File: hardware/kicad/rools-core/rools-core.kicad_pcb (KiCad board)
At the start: 4 copper layers, 50.3 x 128.5 mm, 0 parts

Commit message: Lay out Core front-panel PCB for 10HP Eurorack fit.
Use RK09L 3-pin no-MP pots, split Daisy daughterboard, audio jack refs, and local display footprint library.

Co-authored-by: Cursor <cursoragent@cursor.com>
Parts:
- added C1: 10uF, Capacitor_SMD:C_0603_1608Metric, F.Cu at (121.9, -49.6)
- added C10: 22uF, Capacitor_SMD:C_0805_2012Metric, F.Cu at (143.8, -58.7)
- added C12: 100nF, Capacitor_SMD:C_0603_1608Metric, F.Cu at (169.1, -141.2)
- added C13: 100nF, Capacitor_SMD:C_0603_1608Metric, F.Cu at (169.1, -138.7)
- added C14: 10nF, Capacitor_SMD:C_0603_1608Metric, F.Cu at (169.1, -136.2)
- added C15: 10nF, Capacitor_SMD:C_0603_1608Metric, F.Cu at (169.1, -133.7)
- added C16: 10nF, Capacitor_SMD:C_0603_1608Metric, F.Cu at (169.1, -131.2)
- added C17: 10nF, Capacitor_SMD:C_0603_1608Metric, F.Cu at (169.1, -128.7)
- added C18: 100nF, Capacitor_SMD:C_0603_1608Metric, F.Cu at (169.1, -126.1)
- added C19: 100nF, Capacitor_SMD:C_0603_1608Metric, F.Cu at (169.1, -123.6)
- added C2: 100nF, Capacitor_SMD:C_0603_1608Metric, F.Cu at (121.9, -47.1)
- added C20: 100nF, Capacitor_SMD:C_0603_1608Metric, F.Cu at (201.0, -113.8)
- added C21: 47pF, Capacitor_SMD:C_0603_1608Metric, F.Cu at (109.9, -98.3)
- added C22: 560pF, Capacitor_SMD:C_0603_1608Metric, F.Cu at (109.9, -95.8)
- added C23: 47pF, Capacitor_SMD:C_0603_1608Metric, F.Cu at (109.9, -93.3)
- added C24: 560pF, Capacitor_SMD:C_0603_1608Metric, F.Cu at (109.9, -90.8)
- added C25: 100nF, Capacitor_SMD:C_0603_1608Metric, F.Cu at (109.9, -88.3)
- added C26: 100nF, Capacitor_SMD:C_0603_1608Metric, F.Cu at (109.9, -85.8)
- added C27: 47pF, Capacitor_SMD:C_0603_1608Metric, F.Cu at (109.9, -83.3)
- added C28: 47pF, Capacitor_SMD:C_0603_1608Metric, F.Cu at (109.9, -80.8)
- added C29: 47pF, Capacitor_SMD:C_0603_1608Metric, F.Cu at (109.9, -78.3)
- added C3: 100nF, Capacitor_SMD:C_0603_1608Metric, F.Cu at (121.9, -44.6)
- added C30: 47pF, Capacitor_SMD:C_0603_1608Metric, F.Cu at (113.9, -98.3)
- added C31: 100nF, Capacitor_SMD:C_0603_1608Metric, F.Cu at (113.9, -95.8)
- added C32: 100nF, Capacitor_SMD:C_0603_1608Metric, F.Cu at (113.9, -93.3)
- added C33: 100nF, Capacitor_SMD:C_0603_1608Metric, F.Cu at (169.1, -121.1)
- added C34: 100nF, Capacitor_SMD:C_0603_1608Metric, F.Cu at (173.1, -141.2)
- added C35: 100nF, Capacitor_SMD:C_0603_1608Metric, F.Cu at (173.1, -138.7)
- added C36: 1000uF/25V, Capacitor_SMD:CP_Elec_10x10.5, F.Cu at (127.3, -69.0)
- added C37: 1000uF/25V, Capacitor_SMD:CP_Elec_10x10.5, F.Cu at (127.3, -56.9)
- added C4: 10uF, Capacitor_SMD:C_0603_1608Metric, F.Cu at (121.9, -42.1)
- added C5: 10uF, Capacitor_SMD:C_0603_1608Metric, F.Cu at (121.9, -39.6)
- added C6: 10uF, Capacitor_SMD:C_0603_1608Metric, F.Cu at (121.9, -37.1)
- added C7: 10uF, Capacitor_SMD:C_0603_1608Metric, F.Cu at (121.9, -34.6)
- added C8: 10uF, Capacitor_SMD:C_0603_1608Metric, F.Cu at (125.9, -49.6)
- added C9: 100nF, Capacitor_SMD:C_0603_1608Metric, F.Cu at (125.9, -47.1)
- added D1: SS34, Diode_SMD:D_SMA, F.Cu at (140.5, -48.6)
- added D2: SS34, Diode_SMD:D_SMA, F.Cu at (140.5, -44.1)
- added D3: SS34, Diode_SMD:D_SMA, F.Cu at (140.5, -39.5)
- added FB1: FerriteBead, Inductor_SMD:L_0603_1608Metric, F.Cu at (125.9, -44.6)
- added FB2: FerriteBead, Inductor_SMD:L_0603_1608Metric, F.Cu at (125.9, -42.1)
- added J1: EURO_PWR, Connector_IDC:IDC-Header_2x05_P2.54mm_Vertical, B.Cu at (156.6, 145.9)
- added J2: EXP_BUS, Connector_PinHeader_2.54mm:PinHeader_2x08_P2.54mm_Vertical, B.Cu at (194.1, 125.9)
- added J3: DEBUG_SWD, Connector_PinHeader_2.54mm:PinHeader_1x05_P2.54mm_Vertical, F.Cu at (134.2, -48.6)
- added J4: ST7789, Library:Display_1.54in_240x240, F.Cu at (124.1, 63.7)
- added J_AI_L1: AudioJack2_SwitchT, Connector_Audio:Jack_3.5mm_QingPu_WQP-PJ398SM_Vertical_CircularHoles, F.Cu at (105.6, 144.6)
- added J_AI_R1: AudioJack2_SwitchT, Connector_Audio:Jack_3.5mm_QingPu_WQP-PJ398SM_Vertical_CircularHoles, F.Cu at (117.9, 144.6)
- added J_AO_L1: AudioJack2_SwitchT, Connector_Audio:Jack_3.5mm_QingPu_WQP-PJ398SM_Vertical_CircularHoles, F.Cu at (130.3, 144.6)
- added J_AO_R1: AudioJack2_SwitchT, Connector_Audio:Jack_3.5mm_QingPu_WQP-PJ398SM_Vertical_CircularHoles, F.Cu at (142.6, 144.6)
- added J_CV_IN_1: AudioJack2_SwitchT, Connector_Audio:Jack_3.5mm_QingPu_WQP-PJ398SM_Vertical_CircularHoles, F.Cu at (105.6, 115.9)
- added J_CV_IN_2: AudioJack2_SwitchT, Connector_Audio:Jack_3.5mm_QingPu_WQP-PJ398SM_Vertical_CircularHoles, F.Cu at (117.9, 116.0)
- added J_CV_IN_3: AudioJack2_SwitchT, Connector_Audio:Jack_3.5mm_QingPu_WQP-PJ398SM_Vertical_CircularHoles, F.Cu at (130.3, 115.9)
- added J_CV_IN_4: AudioJack2_SwitchT, Connector_Audio:Jack_3.5mm_QingPu_WQP-PJ398SM_Vertical_CircularHoles, F.Cu at (142.6, 115.9)
- added J_CV_OUT_1: AudioJack2_SwitchT, Connector_Audio:Jack_3.5mm_QingPu_WQP-PJ398SM_Vertical_CircularHoles, F.Cu at (105.6, 130.2)
- added J_CV_OUT_2: AudioJack2_SwitchT, Connector_Audio:Jack_3.5mm_QingPu_WQP-PJ398SM_Vertical_CircularHoles, F.Cu at (117.9, 130.2)
- added J_CV_OUT_3: AudioJack2_SwitchT, Connector_Audio:Jack_3.5mm_QingPu_WQP-PJ398SM_Vertical_CircularHoles, F.Cu at (130.3, 130.2)
- added J_CV_OUT_4: AudioJack2_SwitchT, Connector_Audio:Jack_3.5mm_QingPu_WQP-PJ398SM_Vertical_CircularHoles, F.Cu at (142.6, 130.2)
- added L1: 4.7uH, Inductor_SMD:L_Taiyo-Yuden_NR-40xx, F.Cu at (144.3, -63.0)
- added R1: 330K, Resistor_SMD:R_0603_1608Metric, F.Cu at (125.9, -39.6)
- added R10: 120K, Resistor_SMD:R_0603_1608Metric, F.Cu at (173.1, -128.7)
- added R11: 15K, Resistor_SMD:R_0603_1608Metric, F.Cu at (173.1, -126.1)
- added R12: 120K, Resistor_SMD:R_0603_1608Metric, F.Cu at (173.1, -123.6)
- added R13: 15K, Resistor_SMD:R_0603_1608Metric, F.Cu at (173.1, -121.1)
- added R14: 120K, Resistor_SMD:R_0603_1608Metric, F.Cu at (177.1, -141.2)
- added R15: 120K, Resistor_SMD:R_0603_1608Metric, F.Cu at (177.1, -138.7)
- added R16: 120K, Resistor_SMD:R_0603_1608Metric, F.Cu at (177.1, -136.2)
- added R17: 120K, Resistor_SMD:R_0603_1608Metric, F.Cu at (177.1, -133.7)
- added R18: 120K, Resistor_SMD:R_0603_1608Metric, F.Cu at (177.1, -131.2)
- added R19: 1K, Resistor_SMD:R_0603_1608Metric, F.Cu at (177.1, -128.7)
- added R2: 100K, Resistor_SMD:R_0603_1608Metric, F.Cu at (125.9, -37.1)
- added R20: 1K, Resistor_SMD:R_0603_1608Metric, F.Cu at (177.1, -126.1)
- added R21: 1K, Resistor_SMD:R_0603_1608Metric, F.Cu at (177.1, -123.6)
- added R22: 1K, Resistor_SMD:R_0603_1608Metric, F.Cu at (177.1, -121.1)
- added R23: 200K, Resistor_SMD:R_0603_1608Metric, F.Cu at (181.1, -141.2)
- added R24: 200K, Resistor_SMD:R_0603_1608Metric, F.Cu at (181.1, -138.7)
- added R25: 200K, Resistor_SMD:R_0603_1608Metric, F.Cu at (181.1, -136.2)
- added R26: 200K, Resistor_SMD:R_0603_1608Metric, F.Cu at (181.1, -133.7)
- added R27: 200K, Resistor_SMD:R_0603_1608Metric, F.Cu at (181.1, -131.2)
- added R28: 200K, Resistor_SMD:R_0603_1608Metric, F.Cu at (181.1, -128.7)
- added R29: 200K, Resistor_SMD:R_0603_1608Metric, F.Cu at (181.1, -126.1)
- added R3: 10K, Resistor_SMD:R_0603_1608Metric, F.Cu at (125.9, -34.6)
- added R30: 200K, Resistor_SMD:R_0603_1608Metric, F.Cu at (181.1, -123.6)
- added R31: 33K, Resistor_SMD:R_0603_1608Metric, F.Cu at (181.1, -121.1)
- added R32: 33K, Resistor_SMD:R_0603_1608Metric, F.Cu at (185.1, -141.2)
- added R33: 33K, Resistor_SMD:R_0603_1608Metric, F.Cu at (185.1, -138.7)
- added R34: 33K, Resistor_SMD:R_0603_1608Metric, F.Cu at (185.1, -136.2)
- added R35: 2K, Resistor_SMD:R_0603_1608Metric, F.Cu at (185.1, -133.7)
- added R36: 10K, Resistor_SMD:R_0603_1608Metric, F.Cu at (201.0, -111.3)
- added R37: 10K, Resistor_SMD:R_0603_1608Metric, F.Cu at (201.0, -108.8)
- added R38: 10K, Resistor_SMD:R_0603_1608Metric, F.Cu at (201.0, -106.3)
- added R39: 10K, Resistor_SMD:R_0603_1608Metric, F.Cu at (201.0, -103.8)
- added R4: 73.2K, Resistor_SMD:R_0603_1608Metric, F.Cu at (129.9, -49.6)
- added R40: 10K, Resistor_SMD:R_0603_1608Metric, F.Cu at (201.0, -101.2)
- added R41: 10K, Resistor_SMD:R_0603_1608Metric, F.Cu at (201.0, -98.7)
- added R42: 10K, Resistor_SMD:R_0603_1608Metric, F.Cu at (201.0, -96.2)
- added R43: 22K, Resistor_SMD:R_0603_1608Metric, F.Cu at (129.9, -47.1)
- added R44: 100K, Resistor_SMD:R_0603_1608Metric, F.Cu at (113.9, -90.8)
- added R45: 100K, Resistor_SMD:R_0603_1608Metric, F.Cu at (113.9, -88.3)
- added R46: 100K, Resistor_SMD:R_0603_1608Metric, F.Cu at (113.9, -85.8)
- added R47: 10K, Resistor_SMD:R_0603_1608Metric, F.Cu at (113.9, -83.3)
- added R48: 1K, Resistor_SMD:R_0603_1608Metric, F.Cu at (113.9, -80.8)
- added R49: 100K, Resistor_SMD:R_0603_1608Metric, F.Cu at (113.9, -78.3)
- added R50: 100K, Resistor_SMD:R_0603_1608Metric, F.Cu at (117.9, -98.3)
- added R51: 100K, Resistor_SMD:R_0603_1608Metric, F.Cu at (117.9, -95.8)
- added R52: 10K, Resistor_SMD:R_0603_1608Metric, F.Cu at (117.9, -93.3)
- added R53: 1K, Resistor_SMD:R_0603_1608Metric, F.Cu at (117.9, -90.8)
- added R54: 10K, Resistor_SMD:R_0603_1608Metric, F.Cu at (117.9, -88.3)
- added R55: 10K, Resistor_SMD:R_0603_1608Metric, F.Cu at (117.9, -85.8)
- added R56: 100K, Resistor_SMD:R_0603_1608Metric, F.Cu at (117.9, -83.3)
- added R57: 100K, Resistor_SMD:R_0603_1608Metric, F.Cu at (117.9, -80.8)
- added R58: 100K, Resistor_SMD:R_0603_1608Metric, F.Cu at (117.9, -78.3)
- added R59: 100K, Resistor_SMD:R_0603_1608Metric, F.Cu at (121.9, -98.3)
- added R60: 100K, Resistor_SMD:R_0603_1608Metric, F.Cu at (121.9, -95.8)
- added R61: 100K, Resistor_SMD:R_0603_1608Metric, F.Cu at (121.9, -93.3)
- added R62: 1K, Resistor_SMD:R_0603_1608Metric, F.Cu at (121.9, -90.8)
- added R63: 1K, Resistor_SMD:R_0603_1608Metric, F.Cu at (121.9, -88.3)
- added R64: 10K, Resistor_SMD:R_0603_1608Metric, F.Cu at (129.9, -44.6)
- added R65: 10K, Resistor_SMD:R_0603_1608Metric, F.Cu at (129.9, -42.1)
- added R7: 15K, Resistor_SMD:R_0603_1608Metric, F.Cu at (173.1, -136.2)
- added R8: 120K, Resistor_SMD:R_0603_1608Metric, F.Cu at (173.1, -133.7)
- added R9: 15K, Resistor_SMD:R_0603_1608Metric, F.Cu at (173.1, -131.2)
- added REF**: PinHeader_1x08_P2.54mm_Vertical_SMD_Pin1Right, Connector_PinHeader_2.54mm:PinHeader_1x08_P2.54mm_Vertical_SMD_Pin1Right, B.Cu at (142.4, 64.1)
- added REF**: PinHeader_1x08_P2.54mm_Vertical_SMD_Pin1Right, Connector_PinHeader_2.54mm:PinHeader_1x08_P2.54mm_Vertical_SMD_Pin1Right, B.Cu at (124.1, 99.4)
- added RV1: Knob, Potentiometer_THT:RK09L_3pin_noMP, F.Cu at (105.6, 99.3)
- added RV2: Knob, Potentiometer_THT:RK09L_3pin_noMP, F.Cu at (117.9, 99.3)
- added RV3: Knob, Potentiometer_THT:RK09L_3pin_noMP, F.Cu at (130.3, 99.3)
- added RV4: Knob, Potentiometer_THT:RK09L_3pin_noMP, F.Cu at (142.6, 99.3)
- added SW1: RotaryEncoder_Switch, Rotary_Encoder:RotaryEncoder_Alps_EC11E-Switch_Vertical_H20mm, F.Cu at (110.6, 87.2)
- added SW2: RotaryEncoder_Switch, Rotary_Encoder:RotaryEncoder_Alps_EC11E-Switch_Vertical_H20mm, F.Cu at (137.6, 87.2)
- added SW3: SW_Push, Button_Switch_THT:SW_PUSH_6mm, F.Cu at (124.1, 87.2)
- added U1: AP2112K-3.3, Package_TO_SOT_SMD:SOT-23-5, F.Cu at (144.2, -72.6)
- added U10: LM393, Package_SO:SOIC-8_3.9x4.9mm_P1.27mm, F.Cu at (112.1, -41.6)
- added U2: TPS54302, Package_TO_SOT_SMD:TSOT-23-6, F.Cu at (144.2, -68.0)
- added U4: OPA4171, Package_SO:SOIC-14_3.9x8.7mm_P1.27mm, F.Cu at (112.1, -122.1)
- added U5: MCP6004, Package_SO:SOIC-14_3.9x8.7mm_P1.27mm, F.Cu at (120.5, -122.1)
- added U6: LM4040DBZ-10, Package_TO_SOT_SMD:SOT-23, F.Cu at (136.3, -125.2)
- added U7: TL074, Package_SO:SOIC-14_3.9x8.7mm_P1.27mm, F.Cu at (128.1, -94.3)
- added U8: TL074, Package_SO:SOIC-14_3.9x8.7mm_P1.27mm, F.Cu at (136.6, -94.3)
- added U9: DAC8565, Package_SO:TSSOP-16_4.4x5mm_P0.65mm, F.Cu at (129.5, -124.1)
- added U_Daisy1: ES_DAISY_SEED, Module:Electrosmith_Daisy_Seed, B.Cu at (184.8, 50.3)
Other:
- board size 50.3 x 128.5 mm -> 102 x 108 mm

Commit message: Route Core PCB and place Daisy Seed on the daughterboard.
Sync schematic sheets with the split-board layout and updated interconnects.

Co-authored-by: Cursor <cursoragent@cursor.com>
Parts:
- removed C37: 1000uF/25V, Capacitor_SMD:CP_Elec_10x10.5
- removed REF** (x2): PinHeader_1x08_P2.54mm_Vertical_SMD_Pin1Right, Connector_PinHeader_2.54mm:PinHeader_1x08_P2.54mm_Vertical_SMD_Pin1Right
- added C11: 10uF, Capacitor_SMD:C_0603_1608Metric, B.Cu at (160.2, 108.7)
- added C38: 100nF, Capacitor_SMD:C_0603_1608Metric, B.Cu at (160.2, 110.4)
- added J5: J_BOT_UI, Connector_PinHeader_2.54mm:PinHeader_2x10_P2.54mm_Vertical_SMD, B.Cu at (124.1, 130.9)
- added J6: J_TOP_UI, Connector_PinHeader_2.54mm:PinHeader_2x08_P2.54mm_Vertical_SMD, B.Cu at (124.1, 63.6)
- added J7: J_TOP_MAIN, Connector_PinSocket_2.54mm:PinSocket_2x08_P2.54mm_Vertical_SMD, F.Cu at (176.1, 63.6)
- added J8: J_BOT_MAIN, Connector_PinSocket_2.54mm:PinSocket_2x10_P2.54mm_Vertical_SMD, F.Cu at (176.1, 130.9)
- C10, C20, C33, C34, C35, C4, C5, C7, C8, C9, D1, D2, D3, FB1, FB2, J3, L1, R1, R11, R13, R18, R19, R2, R22, R3, R4, R42, R43, R64, R65, R7, R9, U10, U2, U4, U9: moved to B.Cu
- C36: value 1000uF/25V -> 470uF/25V; footprint Capacitor_SMD:CP_Elec_10x10.5 -> Capacitor_THT:CP_Radial_D8.0mm_P3.50mm; moved to B.Cu
- moved C35 282.3 mm to (196.2, 142.6), turned to 180 degrees
- moved R7 280.4 mm to (184.1, 144.0), turned to 90 degrees
- moved U9 279.7 mm to (188.6, 149.3), turned to -90 degrees
- moved R9 275.4 mm to (186.3, 143.9), turned to 90 degrees
- moved C34 274.8 mm to (195.8, 132.7), turned to 90 degrees
- moved R11 270.9 mm to (192.6, 144.0), turned to 90 degrees
- moved U4 270.8 mm to (188.8, 137.6), turned to 180 degrees
- moved R18 266.4 mm to (181.8, 135.2), turned to 90 degrees
- moved R13 265.7 mm to (189.5, 144.0), turned to 90 degrees
- moved R19 259.9 mm to (190.0, 131.0)
- moved C33 255.0 mm to (194.2, 132.6), turned to 90 degrees
- moved R22 253.2 mm to (183.6, 132.0), turned to 180 degrees
- moved D1 196.9 mm to (160.1, 147.3), turned to 180 degrees
- moved C4 196.0 mm to (165.8, 148.9)
- moved FB1 194.1 mm to (154.8, 147.3)
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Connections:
- net Net-(J_AI_R1-PadS) renamed J_AUDIO_IN_R
- net Net-(J_AO_L1-PadS) renamed J_AUDIO_OUT_L
- net Net-(J_AO_R1-PadS) renamed J_AUDIO_OUT_R
- net Net-(J_CV_IN_1-PadS) renamed J_CV_IN_1
- net Net-(J_CV_IN_2-PadS) renamed J_CV_IN_2
- net Net-(J_CV_IN_3-PadS) renamed J_CV_IN_3
- net Net-(J_CV_IN_4-PadS) renamed J_CV_IN_4
- net Net-(J_CV_OUT_1-PadS) renamed J_CV_OUT_1
- net Net-(J_CV_OUT_2-PadS) renamed J_CV_OUT_2
- net Net-(J_CV_OUT_3-PadS) renamed J_CV_OUT_3
- net Net-(J_CV_OUT_4-PadS) renamed J_CV_OUT_4
- FB1 pad 1: Net-(J1-Pin_10) -> /Power/+12V_IN
- FB2 pad 1: Net-(J1-Pin_2) -> /Power/-12V_IN
- J1 pad 1: unconnected-(J1-Pin_1-Pad1) -> /Power/-12V_IN
- J1 pad 10: Net-(J1-Pin_10) -> /Power/+12V_IN
- J1 pad 2: Net-(J1-Pin_2) -> /Power/-12V_IN
- J1 pad 3: unconnected-(J1-Pin_3-Pad3) -> GND
- J1 pad 4: unconnected-(J1-Pin_4-Pad4) -> GND
- J1 pad 5: unconnected-(J1-Pin_5-Pad5) -> GND
- J1 pad 6: unconnected-(J1-Pin_6-Pad6) -> GND
- J1 pad 7: unconnected-(J1-Pin_7-Pad7) -> GND
- J1 pad 9: unconnected-(J1-Pin_9-Pad9) -> /Power/+12V_IN
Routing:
- net GND: track 0.00 -> 54.3 mm, vias 0 -> 23
- net ENC_A_B: track 0.00 -> 51.9 mm, vias 0 -> 1
- net EXTI_PWR: track 0.00 -> 50.7 mm
- net ENC_A_A: track 0.00 -> 47.6 mm, vias 0 -> 1
- net ENC_A_SW: track 0.00 -> 43.6 mm, vias 0 -> 1
- net BTN_CENTER: track 0.00 -> 41.4 mm, vias 0 -> 1
- net ENC_B_B: track 0.00 -> 36.9 mm
- net +12V_SAFE: track 0.00 -> 36.1 mm
- net +3V3_A: track 0.00 -> 32.2 mm
- net ENC_B_A: track 0.00 -> 29.0 mm
- net SPI1_MOSI: track 0.00 -> 25.8 mm, vias 0 -> 1
- net +3V3_D: track 0.00 -> 25.8 mm
- net SPI1_SCK: track 0.00 -> 25.5 mm, vias 0 -> 1
- net LCD_CS: track 0.00 -> 24.9 mm
- net LCD_RST: track 0.00 -> 23.8 mm
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- added copper zone on In1.Cu, net GND

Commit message: Remove Patch reference assets and continue Core PCB routing.
Drop imported Patch symbols, local display footprint, and stale BOM CSV while advancing layout and schematic interconnects.

Co-authored-by: Cursor <cursoragent@cursor.com>
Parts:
- C1, C12, C13, C19, C2, C21, C22, C23, C24, C25, C26, C27, C28, C29, C3, C30, C31, C32, C6, R10, R12, R14, R15, R16, R17, R20, R21, R35, R36, R37, R38, R39, R40, R41, R44, R45, R46, R47, R48, R49, R50, R51, R52, R53, R54, R55, R56, R57, R58, R59, R60, R61, R62, R63, R8, U1, U6, U7, U8: moved to B.Cu
- moved R35 262.3 mm to (178.3, 128.5)
- moved R15 259.8 mm to (168.8, 121.0), turned to -90 degrees
- moved R14 258.6 mm to (185.4, 117.3), turned to 180 degrees
- moved C12 258.1 mm to (170.7, 116.9), turned to 90 degrees
- moved C13 256.0 mm to (181.4, 117.1), turned to -90 degrees
- moved U6 255.5 mm to (174.3, 127.5), turned to 180 degrees
- moved C19 254.7 mm to (175.3, 131.0), turned to -90 degrees
- moved R8 250.9 mm to (166.5, 117.2)
- moved R16 249.3 mm to (168.8, 113.0), turned to 90 degrees
- moved R17 246.8 mm to (183.0, 113.1), turned to 90 degrees
- moved R10 244.2 mm to (166.5, 115.5)
- moved R33 242.1 mm to (187.6, 103.4), turned to 180 degrees
- moved R34 240.2 mm to (198.3, 103.6)
- moved R12 239.6 mm to (185.3, 115.6), turned to 180 degrees
- moved R20 239.2 mm to (170.4, 113.0), turned to -90 degrees
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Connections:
- J5 pad 10: J_CV_OUT_4 -> J_CV_IN_1
- J5 pad 11: J_CV_IN_1 -> J_CV_OUT_3
- J5 pad 12: J_CV_IN_2 -> J_CV_OUT_2
- J5 pad 13: J_CV_IN_3 -> J_CV_OUT_4
- J5 pad 14: J_CV_IN_4 -> J_CV_OUT_1
- J5 pad 15: IN_L_NORM -> J_AUDIO_OUT_R
- J5 pad 16: J_AUDIO_IN_R -> IN_L_NORM
- J5 pad 18: J_AUDIO_OUT_R -> J_AUDIO_IN_R
- J5 pad 3: KNOB1_ADC -> KNOB3_ADC
- J5 pad 5: KNOB3_ADC -> KNOB4_ADC
- J5 pad 6: KNOB4_ADC -> KNOB1_ADC
- J5 pad 7: J_CV_OUT_1 -> J_CV_IN_3
- J5 pad 8: J_CV_OUT_2 -> J_CV_IN_2
- J5 pad 9: J_CV_OUT_3 -> J_CV_IN_4
- J8 pad 10: J_CV_OUT_4 -> J_CV_IN_1
- J8 pad 11: J_CV_IN_1 -> J_CV_OUT_3
- J8 pad 12: J_CV_IN_2 -> J_CV_OUT_2
- J8 pad 13: J_CV_IN_3 -> J_CV_OUT_4
- J8 pad 14: J_CV_IN_4 -> J_CV_OUT_1
- J8 pad 15: IN_L_NORM -> J_AUDIO_OUT_R
- J8 pad 16: J_AUDIO_IN_R -> IN_L_NORM
- J8 pad 18: J_AUDIO_OUT_R -> J_AUDIO_IN_R
- J8 pad 3: KNOB1_ADC -> KNOB3_ADC
- J8 pad 5: KNOB3_ADC -> KNOB4_ADC
- J8 pad 6: KNOB4_ADC -> KNOB1_ADC
- J8 pad 7: J_CV_OUT_1 -> J_CV_IN_3
- J8 pad 8: J_CV_OUT_2 -> J_CV_IN_2
- J8 pad 9: J_CV_OUT_3 -> J_CV_IN_4
- U9 pad 1: DAC_A -> DAC_D
- U9 pad 2: DAC_B -> DAC_C
- U9 pad 7: DAC_C -> DAC_B
- U9 pad 8: DAC_D -> DAC_A
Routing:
- net -10V_REF: track 0.00 -> 122.2 mm, vias 0 -> 6
- net +3V3_D: track 25.8 -> 112.2 mm, vias 0 -> 13
- net KNOB4_ADC: track 3.96 -> 66.5 mm
- net +3V3_A: track 32.2 -> 89.0 mm, vias 0 -> 3
- net -12V: track 17.7 -> 71.1 mm, vias 1 -> 5
- net EXTI_PWR: track 50.7 -> 2.30 mm
- net KNOB1_ADC: track 6.98 -> 52.6 mm
- net ENC_B_SW: track 6.92 -> 46.7 mm, vias 0 -> 2
- net IN_L_NORM: track 0.00 -> 37.5 mm
- net KNOB2_ADC: track 2.38 -> 39.1 mm
- net GND: track 54.3 -> 91.0 mm, vias 23 -> 40
- net KNOB3_ADC: track 8.73 -> 43.8 mm
- net +12V: track 16.0 -> 45.7 mm, vias 1 -> 5
- net +5V: track 10.0 -> 39.2 mm, vias 1 -> 2
- net LCD_BLK: track 6.68 -> 35.5 mm, vias 0 -> 1
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- added copper zone on In2.Cu, net +3V3_A
- added copper zone on In2.Cu, net +3V3_D

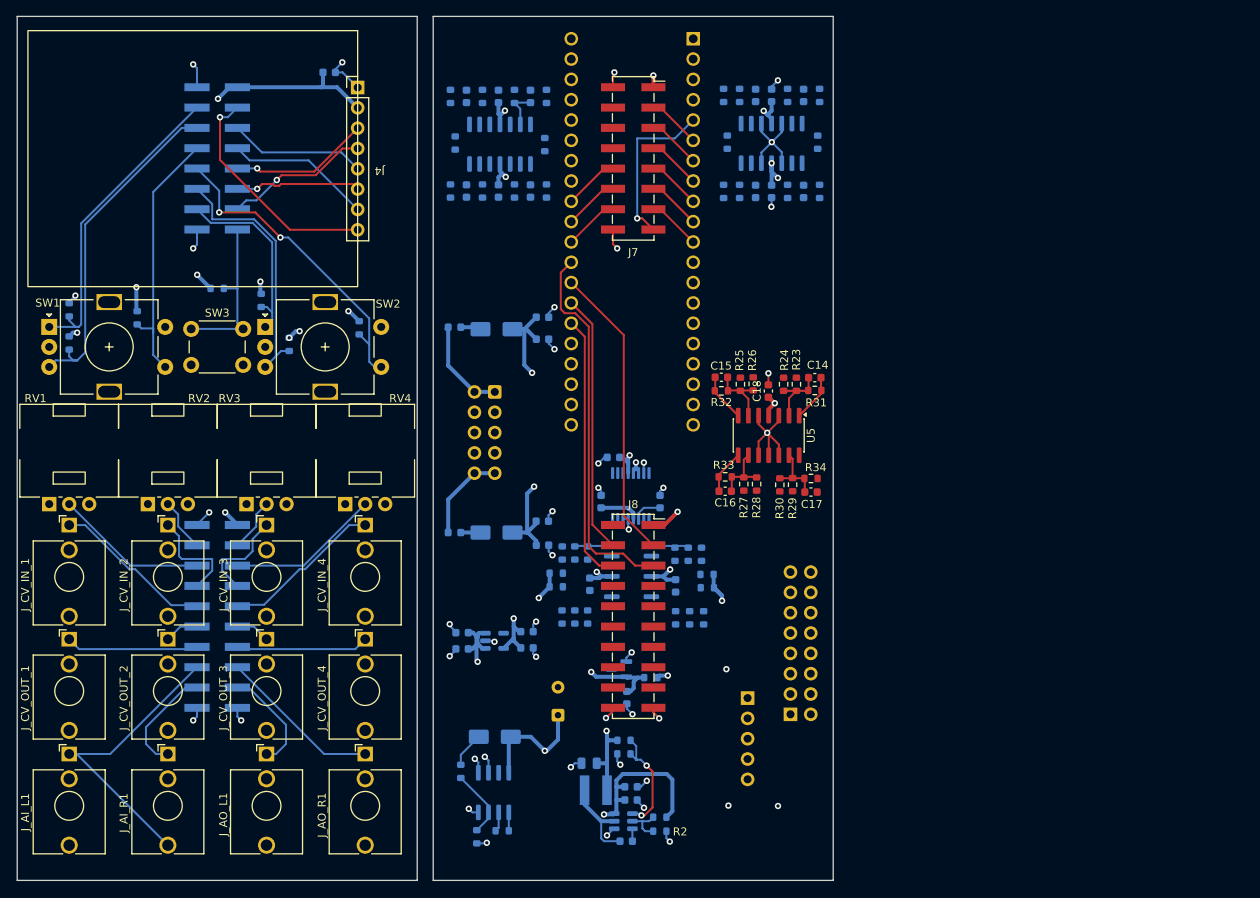
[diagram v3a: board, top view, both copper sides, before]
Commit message: Align seed schematic with Electrosmith Daisy module footprint.
Update power and UI interconnects and continue Core PCB layout after removing the local footprint library.

Co-authored-by: Cursor <cursoragent@cursor.com>
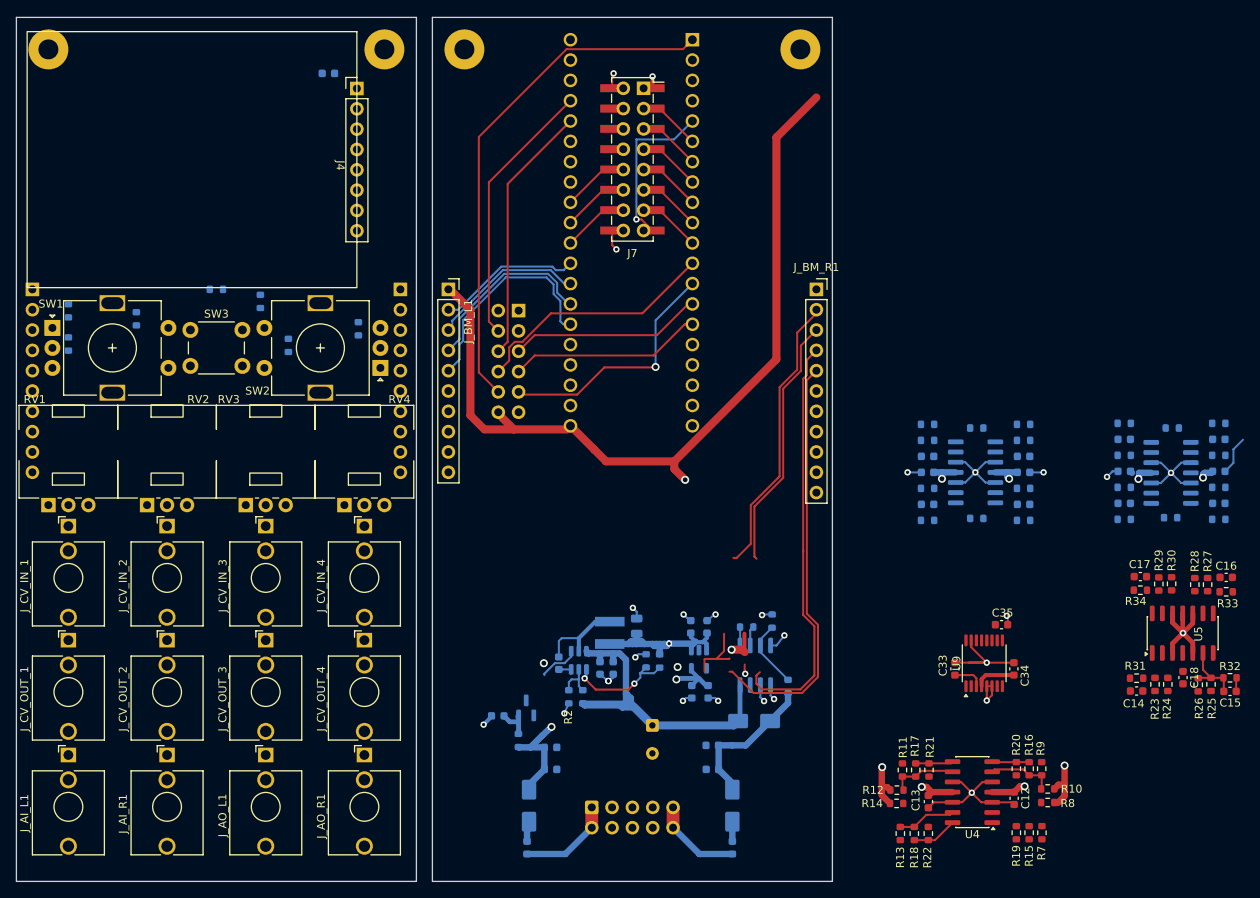
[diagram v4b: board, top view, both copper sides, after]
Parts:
- removed J3: DEBUG_SWD, Connector_PinHeader_2.54mm:PinHeader_1x05_P2.54mm_Vertical
- removed J5: J_BOT_UI, Connector_PinHeader_2.54mm:PinHeader_2x10_P2.54mm_Vertical_SMD
- removed J8: J_BOT_MAIN, Connector_PinSocket_2.54mm:PinSocket_2x10_P2.54mm_Vertical_SMD
- added J_BM_L1: Conn_01x10_Pin, Connector_PinSocket_2.54mm:PinSocket_1x10_P2.54mm_Vertical, F.Cu at (153.0, 80.0)
- added J_BM_R1: Conn_01x10_Pin, Connector_PinSocket_2.54mm:PinSocket_1x11_P2.54mm_Vertical, F.Cu at (199.0, 80.0)
- added J_BU_L1: Conn_01x10_Pin, Connector_PinHeader_2.54mm:PinHeader_1x10_P2.54mm_Vertical, B.Cu at (101.0, 80.0)
- added J_BU_R1: Conn_01x10_Pin, Connector_PinHeader_2.54mm:PinHeader_1x10_P2.54mm_Vertical, B.Cu at (147.0, 80.0)
- added REF**: MountingHole_2.5mm_Pad, MountingHole:MountingHole_2.5mm_Pad, F.Cu at (145.0, 50.0)
- added REF**: MountingHole_2.5mm_Pad, MountingHole:MountingHole_2.5mm_Pad, F.Cu at (155.0, 50.0)
- added REF**: MountingHole_2.5mm_Pad, MountingHole:MountingHole_2.5mm_Pad, F.Cu at (103.0, 50.0)
- added REF**: MountingHole_2.5mm_Pad, MountingHole:MountingHole_2.5mm_Pad, F.Cu at (197.0, 50.0)
- C12, C13, C33, C34, C35, R10, R11, R12, R13, R14, R15, R16, R17, R18, R19, R20, R21, R22, R7, R8, R9, U4, U9: moved to F.Cu
- J2: footprint Connector_PinHeader_2.54mm:PinHeader_2x08_P2.54mm_Vertical -> Connector_PinHeader_2.54mm:PinHeader_2x06_P2.54mm_Vertical
- J6: footprint Connector_PinHeader_2.54mm:PinHeader_2x08_P2.54mm_Vertical_SMD -> Connector_PinHeader_2.54mm:PinHeader_2x08_P2.54mm_Vertical
- moved R63 104.4 mm to (249.3, 96.7), turned to 0 degrees
- moved C30 103.4 mm to (249.3, 98.7), turned to 0 degrees
- moved R61 102.4 mm to (249.3, 100.7), turned to 0 degrees
- moved C32 101.5 mm to (249.3, 102.7), turned to 0 degrees
- moved R60 100.7 mm to (249.3, 104.7), turned to 0 degrees
- moved C29 100.0 mm to (249.3, 106.7), turned to 0 degrees
- moved R62 99.3 mm to (249.3, 108.7), turned to 0 degrees
- moved R59 96.5 mm to (243.5, 97.3), turned to 0 degrees
- moved U8 93.4 mm to (243.3, 102.9), turned to 0 degrees
- moved R58 91.1 mm to (243.3, 108.5), turned to 0 degrees
- moved R55 89.1 mm to (237.5, 96.7), turned to 0 degrees
- moved C28 87.9 mm to (237.5, 98.7), turned to 0 degrees
- moved R57 86.8 mm to (237.5, 100.7), turned to 0 degrees
- moved C31 85.7 mm to (237.5, 102.7), turned to 0 degrees
- moved R56 84.7 mm to (237.5, 104.7), turned to 0 degrees
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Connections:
- J2 pad 1: +3V3_D -> +5V
- J2 pad 10: USB_D+ -> EXP_GPIO0
- J2 pad 11: +5V -> GND
- J2 pad 12: GND -> +3V3_A
- J2 pad 2: +3V3_A -> +3V3_D
- J2 pad 3: SWDIO -> GND
- J2 pad 4: SWCLK -> USB_D+
- J2 pad 5: RESET -> MIDI_TX
- J2 pad 6: GND -> USB_D-
- J2 pad 7: MIDI_TX -> MIDI_RX
- J2 pad 8: MIDI_RX -> I2C_SCL
- J2 pad 9: USB_D- -> I2C_SDA
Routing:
- net +3V3_D: track 112.2 -> 6.40 mm, vias 13 -> 3
- net -10V_REF: track 122.2 -> 18.3 mm, vias 6 -> 2
- net +5V: track 39.2 -> 110.5 mm, vias 2 -> 1
- net EXP_GPIO0: track 0.00 -> 64.6 mm
- net KNOB4_ADC: track 66.5 -> 18.0 mm
- net -12V: track 71.1 -> 23.1 mm, vias 5 -> 4
- net +3V3_A: track 89.0 -> 133.6 mm, vias 3 -> 2
- net ENC_A_B: track 42.3 -> 0.00 mm
- net ENC_B_SW: track 46.7 -> 6.92 mm, vias 2 -> 0
- net ENC_A_A: track 39.3 -> 0.00 mm
- net J_CV_IN_2: track 12.9 -> 52.0 mm
- net IN_L_NORM: track 37.5 -> 0.00 mm
- net USB_D+: track 0.00 -> 33.5 mm
- net ENC_A_SW: track 32.9 -> 0.00 mm
- net USB_D-: track 0.00 -> 32.5 mm
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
